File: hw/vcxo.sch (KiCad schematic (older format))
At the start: 68 parts, among them P1 CONN_01X04, P2 BNC, P3 CONN_01X02, Q1 Q_NPN_BCE, Q2 Q_NPN_BCE, U1 DAC1220E, U2 ISL60002, U3 TCVCXO_LFTVXO076344, U4 AP1117D33, U5 LTC6752HS5, U6 SN74LVC2G74, Y1 2MHz

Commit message: removed thrash
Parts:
- removed Q1, Q2: Q_NPN_BCE, symbol Q_NPN_BCE
- added U7, U8: BF776, symbol BF776
- C1, C10, C11, C12, C13, C14, C15, C16, C17, C18, C19, C2, C20, C21, C22, C23, C24, C25, C26, C27, C28, C29, C3, C31, C33, C35, C36, C37, C38, C39, C4, C5, C6, C8: footprint (none) -> Capacitors_SMD:C_0805_HandSoldering
- C30, C32, C7, C9: footprint (none) -> Capacitors_THT:C_Disc_D9.0mm_W2.5mm_P5.00mm
- C34: footprint (none) -> Capacitors_SMD:CP_Elec_4x5.8
- D1, D2: footprint (none) -> Diodes_THT:D_5W_P5.08mm_Vertical_KathodeUp
- L1, L3, L7, L8: footprint (none) -> Inductors_SMD:L_Taiyo-Yuden_NR-30xx_HandSoldering
- L2, L4: footprint (none) -> Inductors_SMD:L_0805_HandSoldering
- L5, L6: footprint (none) -> Inductors_SMD:L_0603_HandSoldering
- P1: footprint (none) -> Pin_Headers:Pin_Header_Straight_1x04_Pitch2.54mm
- P2: footprint (none) -> SMA:SMA_sidemount
- P3: footprint (none) -> Pin_Headers:Pin_Header_Straight_1x02_Pitch2.54mm
- R1, R3, R5: footprint (none) -> Resistors_SMD:R_1206_HandSoldering
- R2, R4, R6, R7: footprint (none) -> Resistors_SMD:R_0805_HandSoldering
- U1: footprint MODULE -> Housings_SSOP:SSOP-16_3.9x4.9mm_Pitch0.635mm
- U2: footprint MODULE -> TO_SOT_Packages_SMD:SOT-23
- U3: footprint MODULE -> LFTVXO076344:LFTVXO076344
- U4: footprint (none) -> TO_SOT_Packages_SMD:SOT-223-3_TabPin2
- U5: footprint MODULE -> TO_SOT_Packages_SMD:SOT-23-5_HandSoldering
- U6: footprint MODULE -> Housings_SSOP:VSSOP-8_2.3x2mm_Pitch0.5mm
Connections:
- wire segments 76 -> 88

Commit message: created pcb
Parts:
- removed C18: 10u, Capacitors_SMD:C_0805_HandSoldering, symbol C
- removed C20: 100n, Capacitors_SMD:C_0805_HandSoldering, symbol C_Small
- added J1, J2, J3, J4, J5, J6: Conn_01x01, Pin_Headers:Pin_Header_Straight_1x01_Pitch2.00mm, symbol Conn_01x01
- D1: footprint Diodes_THT:D_5W_P5.08mm_Vertical_KathodeUp -> Pin_Headers:Pin_Header_Straight_1x02_Pitch2.54mm
- D2: footprint Diodes_THT:D_5W_P5.08mm_Vertical_KathodeUp -> Diodes_SMD:D_SOD-523
- U7, U8: footprint (none) -> SOT343:SOT343
- Y1: footprint (none) -> Crystals:Crystal_HC18-U_Vertical
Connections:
- net labels removed: VCC
- wire segments 88 -> 109
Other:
- moved on the sheet: C23, C27, D2, P3

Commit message: fixed one cap value
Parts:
- C15: value 10n -> 100n
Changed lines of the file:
@@
 P 6750 4450
 F 0 "C15" H 6760 4520 50  0000 L CNN
-F 1 "10n" H 6760 4370 50  0000 L CNN
+F 1 "100n" H 6760 4370 50  0000 L CNN
 F 2 "Capacitors_SMD:C_0805_HandSoldering" H 6750 4450 60  0001 C CNN
 F 3 "" H 6750 4450 60  0000 C CNN

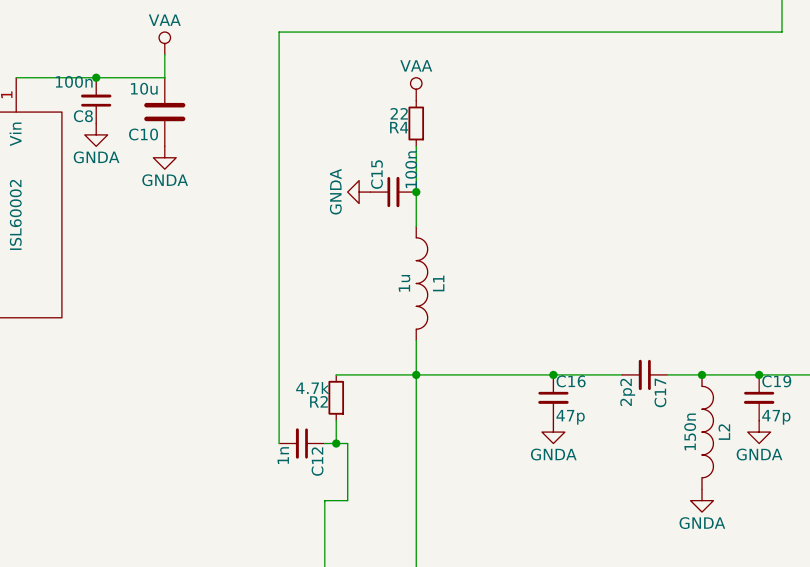
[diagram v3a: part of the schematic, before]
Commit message: fixed some L value
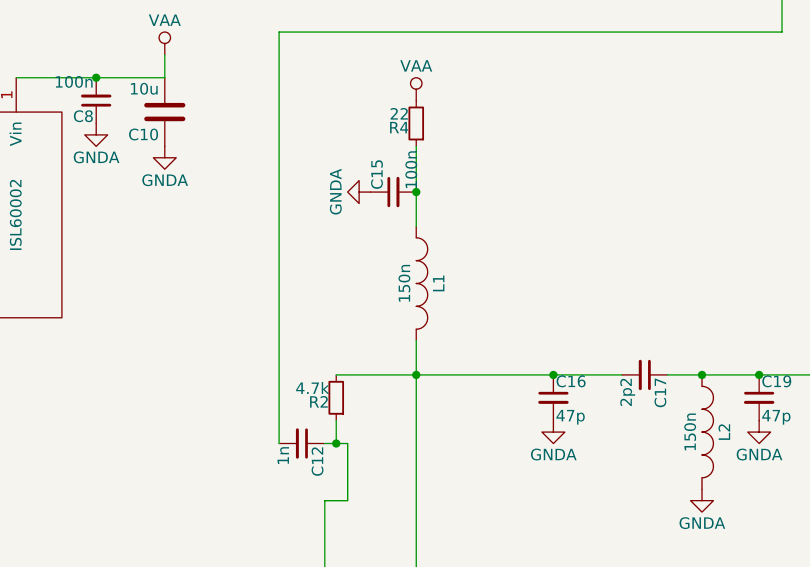
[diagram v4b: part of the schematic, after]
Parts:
- L1: value 1u -> 150n
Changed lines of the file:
@@
 P 6850 4850
 F 0 "L1" H 6850 4950 50  0000 C CNN
-F 1 "1u" H 6850 4800 50  0000 C CNN
+F 1 "150n" H 6850 4800 50  0000 C CNN
 F 2 "Inductors_SMD:L_Taiyo-Yuden_NR-30xx_HandSoldering" H 6850 4850 60  0001 C CNN
 F 3 "" H 6850 4850 60  0000 C CNN
